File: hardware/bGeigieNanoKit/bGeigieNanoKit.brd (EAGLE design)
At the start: 104.8 x 66.7 mm, 41 parts, among them T1 2SC1815

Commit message: before removing second lcd
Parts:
- JP2: device SparkFun:1X02 -> microbuilder:1X04_ROUND
- LCD: value SSD1306_128X64_V2_LCD1.3IN_TOP -> SSD1306_128X64_V2_LCD1.3IN_LEVER; device open_hw_sockets:SSD1306_128X64_1.3IN_LCD_TOP -> open_hw_sockets:SSD1306_128X64_1.3IN_LCD_LEVER
- LCD2: value SSD1306_128X64_V2_LCD0.96IN_MIN -> SSD1306_128X64_V2_LCD0.96IN_MNT_NOOUT; device open_hw_sockets:SSD1306_128X64_0.96IN_MIN_LCD -> open_hw_sockets:SSD1306_128X64_0.96IN_LCD_MNT_NOOUT
- R8: value 47k -> 10k
- R9: value 1k -> 2.2k
- S1: device open_hw_sockets:EG1218 -> adafruit:EG1218
- moved C1 9.84 mm to (92.4, 3.17), turned to 0 degrees
- moved R9 8.82 mm to (29.8, 24.1), turned to 0 degrees
- moved JP2 6.93 mm to (18.4, 21.3)
- moved R12 4.77 mm to (61.6, 3.17)
- moved D1 3.62 mm to (42.2, 14.6)
- moved R10 3.49 mm to (45.7, 16.8)
- moved R11 3.24 mm to (86.7, 30.8)
- moved JP7 2.93 mm to (89.2, 27.3), turned to 180 degrees
- moved JP1 2.84 mm to (94.0, 11.4)
- moved SG1 1.80 mm to (28.6, 16.8)
- moved LCD 1.53 mm to (42.5, 17.7)
- moved R8 1.42 mm to (29.8, 26.7)
- moved LCD2 1.02 mm to (39.3, 16.2)
- moved C2 0.71 mm to (38.1, 40.6)
- moved U$5 0.51 mm to (79.2, 67.3)
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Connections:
- removed net N$21: FIO.JP5$12, JP4.6
- new net N$41: FIO.JP5$14, JP4.8
- net GND: now also LCD2.U$24$P$1, LCD2.U$25$P$1; no longer LCD.U$24$P$1, LCD.U$25$P$1
- net N$14: now also FIO.JP5$12, JP4.6; no longer FIO.JP5$14, JP4.8
- net N$15: no longer R4.1
- net N$33: now also R4.1
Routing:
- net N$33: track 5.72 -> 33.8 mm
- net N$15: track 27.2 -> 6.35 mm
- net VCC: track 219.5 -> 210.8 mm
- net N$14: track 24.6 -> 30.5 mm
- net N$41: track 0.00 -> 5.72 mm
- net N$21: track 5.72 -> 0.00 mm
- net N$26: track 3.49 -> 8.94 mm
- net N$20: track 47.8 -> 52.7 mm
- net N$23: track 11.8 -> 16.6 mm
- net N$29: track 11.3 -> 6.71 mm
- net N$31: track 6.88 -> 3.31 mm
- net N$24: track 9.42 -> 12.8 mm
- net N$25: track 16.9 -> 14.4 mm
- net N$32: track 51.9 -> 53.7 mm
- net N$4: track 37.4 -> 35.8 mm
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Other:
- board text added: "Audio"
- board text added: "bGeigie Nano Kit v1.0r2"
- board text removed: "Audio Out"
- board text removed: "bGeigie Nano Kit v1.0"

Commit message: applied most all changes rc v1.0r2
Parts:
- removed CHARGE: RED, adafruit:LED3MM
- removed JP7: (no value), microbuilder:JUMPER2
- removed LCD2: SSD1306_128X64_V2_LCD0.96IN_MNT_NOOUT, open_hw_sockets:SSD1306_128X64_0.96IN_LCD_MNT_NOOUT
- removed R11: 1k, rcl:0207/10
- added U$1: (no value), open_hw_sockets:SAFECAST_LOGO4
- C1, C2, C3: device rcl:C050-024X044 -> rcl:C025-024X044
- moved JP2 5.08 mm to (18.4, 16.2)
- moved C3 3.49 mm to (47.3, 25.7)
- moved C2 3.18 mm to (36.2, 43.2), turned to 90 degrees
- moved SG1 2.88 mm to (31.4, 16.5)
- moved D1 1.93 mm to (41.9, 16.5)
- moved C1 1.59 mm to (93.3, 4.45)
- moved S5 1.14 mm to (7.30, 14.0)
- moved JP1 1.14 mm to (94.6, 12.4)
- moved LCD 0.70 mm to (43.2, 17.7)
- moved JP4 0.32 mm to (59.7, 49.8)
- turned R4 to 90 degrees
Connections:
- removed net N$29: JP7.1, R11.1
- removed net N$31: CHARGE.K, R11.2
- net GND: no longer JP7.2, LCD2.JP1$8, LCD2.U$24$P$1, LCD2.U$25$P$1
- net N$1: no longer LCD2.JP1$1
- net N$2: no longer LCD2.JP1$2
- net N$3: no longer LCD2.JP1$3
- net N$4: no longer LCD2.JP1$5
- net N$5: no longer LCD2.JP1$4
- net VCC: no longer LCD2.JP1$7
- net VIN: no longer CHARGE.A
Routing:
- net N$17: track 31.5 -> 21.8 mm
- net N$29: track 6.71 -> 0.00 mm
- net VIN: track 17.4 -> 12.6 mm
- net N$27: track 30.4 -> 26.3 mm
- net N$31: track 3.31 -> 0.00 mm
- net N$24: track 12.8 -> 15.4 mm
- net N$23: track 16.6 -> 14.3 mm
- net N$18: track 76.4 -> 74.2 mm
- net N$25: track 14.4 -> 16.5 mm
- net N$33: track 33.8 -> 35.2 mm
- net N$32: track 53.7 -> 52.5 mm
- net N$20: track 52.7 -> 51.6 mm
- net N$4: track 35.8 -> 35.1 mm
- net N$2: track 42.3 -> 41.6 mm
- net N$5: track 32.5 -> 31.8 mm
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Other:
- board text added: "Audio out"
- board text added: "Special thanks to: Joe,Rob,Jurgen,Sean,Robin,Akiba,Azby Shigeru,Joi,Dan,Peter,Joseph,Medcom,Loftwork,FabCafe Pelican,Tokyo Hacker Space,CRASH Space,Adafruit,Sparkfun"
- board text added: "bGeigie Nano Kit"
- board text added: "bGeigie Nano v1.0r2"
- board text removed: "Audio"
- board text removed: "Special thanks to: Joe, Rob, Jurgen, Sean, Robin, Akiba, Shigeru, Joi, Dan, Medcom, Loftwork, FabCafe, Pelican, Tokyo Hacker Space, CRASH Space, Adafruit, Sparkfun"
- board text removed: "bGeigie Nano Kit v1.0r2"

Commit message: finishing change set for rev2
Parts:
- S1: value (none) -> EG1206; device adafruit:EG1218 -> open_hw_sockets:EG1206
- moved S1 2.13 mm to (90.8, 62.5)
- moved OPENLOG 0.64 mm to (86.7, 25.1)
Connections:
- removed net VIN: FIO.JP6$2
- net GND: now also S1.MT1, S1.MT2
- net N$12: now also S1.2; no longer S1.P
- net N$13: now also S1.3; no longer S1.S
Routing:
- net VIN: track 12.6 -> 0.00 mm
- net VCC: track 211.0 -> 210.4 mm
- net N$9: track 31.2 -> 30.6 mm
- net N$8: track 34.8 -> 34.2 mm
- net N$10: track 27.6 -> 27.0 mm
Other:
- board text added: "bGeigie Nano Kit v1.0r2"
- board text removed: "bGeigie Nano v1.0r2"
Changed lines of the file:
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@@
 <layer number="29" name="tStop" color="7" fill="3" visible="yes" active="yes"/>
 <layer number="30" name="bStop" color="7" fill="6" visible="yes" active="yes"/>
-<layer number="31" name="tCream" color="7" fill="4" visible="yes" active="yes"/>
-<layer number="32" name="bCream" color="7" fill="5" visible="yes" active="yes"/>
+<layer number="31" name="tCream" color="7" fill="4" visible="no" active="yes"/>
+<layer number="32" name="bCream" color="7" fill="5" visible="no" active="yes"/>
 <layer number="33" name="tFinish" color="6" fill="3" visible="yes" active="yes"/>
 <layer number="34" name="bFinish" color="6" fill="6" visible="yes" active="yes"/>
-<layer number="35" name="tGlue" color="7" fill="4" visible="yes" active="yes"/>
-<layer number="36" name="bGlue" color="7" fill="5" visible="yes" active="yes"/>
+<layer number="35" name="tGlue" color="7" fill="4" visible="no" active="yes"/>
+<layer number="36" name="bGlue" color="7" fill="5" visible="no" active="yes"/>
 <layer number="37" name="tTest" color="7" fill="1" visible="yes" active="yes"/>
 <layer number="38" name="bTest" color="7" fill="1" visible="yes" active="yes"/>
@@
 <vertex x="38.1" y="40.64"/>
 </polygon>
-<text x="8.5725" y="57.4675" size="2.54" layer="22" font="vector" ratio="10" distance="40" rot="SMR270">bGeigie Nano v1.0r2</text>
+<text x="7.9375" y="58.1025" size="2.54" layer="22" font="vector" ratio="10" distance="40" rot="SMR270">bGeigie Nano Kit v1.0r2</text>
 </plain>
 <attributes>
@@
 </element>
 <element name="S5" library="SparkFun" package="TACTILE-PTH" value="" x="7.3025" y="13.97" smashed="yes" rot="R180"/>
-<element name="S1" library="adafruit" package="EG1218" value="" x="88.9" y="63.5" smashed="yes" rot="SR180">
-<attribute name="NAME" x="89.789" y="60.6425" size="1.27" layer="25" font="vector" rot="SR180"/>
-</element>
 <element name="SG1" library="SparkFun" package="BUZZER-12MM" value="BUZZER" x="31.4325" y="16.51" smashed="yes" rot="R180">
 <attribute name="NAME" x="33.972503125" y="13.97" size="0.6096" layer="25" ratio="10" rot="R180" display="off"/>
@@
 <attribute name="VALUE" x="34.29" y="53.848" size="1.27" layer="27" ratio="10" display="off"/>
 </element>
-<element name="OPENLOG" library="open_hw_sockets" package="OPENLOG" value="OPENLOG" x="87.3125" y="25.0825" smashed="yes" rot="R270">
-<attribute name="NAME" x="96.9645" y="23.8125" size="2.54" layer="25" rot="SR270" display="off"/>
+<element name="OPENLOG" library="open_hw_sockets" package="OPENLOG" value="OPENLOG" x="86.6775" y="25.0825" smashed="yes" rot="R270">
+<attribute name="NAME" x="96.3295" y="23.8125" size="2.54" layer="25" rot="SR270" display="off"/>
 </element>
 <element name="SW1" library="special" package="EDG-02" value="" x="17.145" y="64.135" smashed="yes" rot="SR90">
@@
 </element>
 <element name="U$1" library="open_hw_sockets" package="SAFECAST_LOGO4" value="" x="50.8" y="50.8" rot="MR270"/>
+<element name="S1" library="open_hw_sockets" package="EG1206" value="EG1206" x="90.805" y="62.5475" rot="R180"/>
 </elements>
 <signals>
@@
 </polygon>
 <contactref element="JP2" pad="2"/>
+<contactref element="S1" pad="MT1"/>
+<contactref element="S1" pad="MT2"/>
 </signal>
 <signal name="VCC" class="1">
@@
 <wire x1="68.58" y1="60.96" x2="69.85" y2="59.69" width="1.4224" layer="1"/>
 <wire x1="69.85" y1="59.69" x2="69.85" y2="55.88" width="1.4224" layer="1"/>
-<wire x1="85.4075" y1="16.1925" x2="88.5825" y2="16.1925" width="1.4224" layer="16"/>
+<wire x1="85.4075" y1="16.1925" x2="87.9475" y2="16.1925" width="1.4224" layer="16"/>
 <wire x1="29.845" y1="38.4175" x2="29.845" y2="41.275" width="1.4224" layer="16"/>
 <wire x1="29.845" y1="41.275" x2="26.67" y2="44.45" width="1.4224" layer="16"/>
@@
 <wire x1="52.832" y1="9.525" x2="57.785" y2="9.525" width="1.4224" layer="1"/>
 <wire x1="77.47" y1="7.62" x2="86.0425" y2="16.1925" width="1.4224" layer="1"/>
-<wire x1="86.0425" y1="16.1925" x2="88.5825" y2="16.1925" width="1.4224" layer="1"/>
+<wire x1="86.0425" y1="16.1925" x2="87.9475" y2="16.1925" width="1.4224" layer="1"/>
 <wire x1="85.4075" y1="16.1925" x2="78.74" y2="22.86" width="1.4224" layer="16"/>
 <wire x1="78.74" y1="22.86" x2="78.74" y2="29.21" width="1.4224" layer="16"/>
@@
 <wire x1="97.155" y1="8.5725" x2="97.155" y2="12.065" width="1.4224" layer="1"/>
 <wire x1="97.155" y1="12.065" x2="93.0275" y2="16.1925" width="1.4224" layer="1"/>
-<wire x1="93.0275" y1="16.1925" x2="88.5825" y2="16.1925" width="1.4224" layer="1"/>
+<wire x1="93.0275" y1="16.1925" x2="87.9475" y2="16.1925" width="1.4224" layer="1"/>
 <wire x1="97.155" y1="8.5725" x2="97.155" y2="6.985" width="1.4224" layer="1"/>
 <wire x1="97.155" y1="6.985" x2="94.615" y2="4.445" width="1.4224" layer="1"/>
@@
 <contactref element="OPENLOG" pad="JP1$3"/>
 <wire x1="59.69" y1="33.02" x2="73.9775" y2="18.7325" width="0.6096" layer="1"/>
-<wire x1="73.9775" y1="18.7325" x2="88.5825" y2="18.7325" width="0.6096" layer="1"/>
+<wire x1="73.9775" y1="18.7325" x2="87.9475" y2="18.7325" width="0.6096" layer="1"/>
 </signal>
 <signal name="N$9">
@@
 <contactref element="OPENLOG" pad="JP1$2"/>
 <wire x1="62.23" y1="33.02" x2="73.9775" y2="21.2725" width="0.6096" layer="1"/>
-<wire x1="73.9775" y1="21.2725" x2="88.5825" y2="21.2725" width="0.6096" layer="1"/>
+<wire x1="73.9775" y1="21.2725" x2="87.9475" y2="21.2725" width="0.6096" layer="1"/>
 </signal>
 <signal name="N$10">
@@
 <contactref element="OPENLOG" pad="JP1$1"/>
 <wire x1="64.77" y1="33.02" x2="73.9775" y2="23.8125" width="0.6096" layer="1"/>
-<wire x1="73.9775" y1="23.8125" x2="88.5825" y2="23.8125" width="0.6096" layer="1"/>
+<wire x1="73.9775" y1="23.8125" x2="87.9475" y2="23.8125" width="0.6096" layer="1"/>
 </signal>
 <signal name="N$12" class="2">
 <contactref element="FIO" pad="JP7$2"/>
-<contactref element="S1" pad="P"/>
-<wire x1="82.55" y1="47.625" x2="82.55" y2="53.34" width="1.4224" layer="1"/>
-<wire x1="82.55" y1="53.34" x2="88.9" y2="59.69" width="1.4224" layer="1"/>
-<wire x1="88.9" y1="59.69" x2="88.9" y2="63.5" width="1.4224" layer="1"/>
-</signal>
-<signal name="VIN">
-<contactref element="FIO" pad="JP6$2"/>
-<wire x1="93.98" y1="41.91" x2="92.71" y2="41.91" width="0.6096" layer="1"/>
-<wire x1="92.71" y1="41.91" x2="91.44" y2="40.64" width="0.6096" layer="1"/>
-<wire x1="91.44" y1="40.64" x2="91.44" y2="35.56" width="0.6096" layer="1"/>
-<wire x1="91.44" y1="35.56" x2="94.615" y2="32.385" width="0.6096" layer="1"/>
+<wire x1="90.805" y1="55.88" x2="82.55" y2="47.625" width="1.4224" layer="1"/>
+<contactref element="S1" pad="2"/>
+<wire x1="90.805" y1="55.88" x2="90.805" y2="62.5475" width="1.4224" layer="1"/>
 </signal>
 <signal name="VBATT">
 <contactref element="FIO" pad="JP2$2"/>
 <contactref element="R1" pad="1"/>
-<wire x1="93.98" y1="50.8" x2="85.725" y2="59.055" width="0.6096" layer="16"/>
-<wire x1="85.725" y1="59.055" x2="66.04" y2="59.055" width="0.6096" layer="16"/>
 <contactref element="JP6" pad="1"/>
 <via x="76.2" y="26.67" extent="1-16" drill="0.6"/>
@@
 <wire x1="85.09" y1="43.18" x2="92.71" y2="50.8" width="0.6096" layer="1"/>
 <wire x1="92.71" y1="50.8" x2="93.98" y2="50.8" width="0.6096" layer="1"/>
+<wire x1="66.04" y1="59.055" x2="76.835" y2="59.055" width="0.6096" layer="16"/>
+<wire x1="76.835" y1="59.055" x2="85.09" y2="50.8" width="0.6096" layer="16"/>
+<wire x1="85.09" y1="50.8" x2="93.98" y2="50.8" width="0.6096" layer="16"/>
 </signal>
 <signal name="N$13" class="2">
 <contactref element="FIO" pad="JP7$1"/>
-<contactref element="S1" pad="S"/>
-<wire x1="86.36" y1="63.5" x2="86.36" y2="62.23" width="1.4224" layer="1"/>
-<wire x1="86.36" y1="62.23" x2="80.01" y2="55.88" width="1.4224" layer="1"/>
-<wire x1="80.01" y1="47.625" x2="80.01" y2="55.88" width="1.4224" layer="1"/>
+<wire x1="87.805" y1="57.325" x2="80.01" y2="49.53" width="1.4224" layer="1"/>
+<wire x1="80.01" y1="49.53" x2="80.01" y2="47.625" width="1.4224" layer="1"/>
+<contactref element="S1" pad="3"/>
+<wire x1="87.805" y1="57.325" x2="87.805" y2="62.5475" width="1.4224" layer="1"/>
 </signal>
 <signal name="N$11">
@@
 </signal>
 </signals>
+<errors>
+</errors>
 </board>
 </drawing>

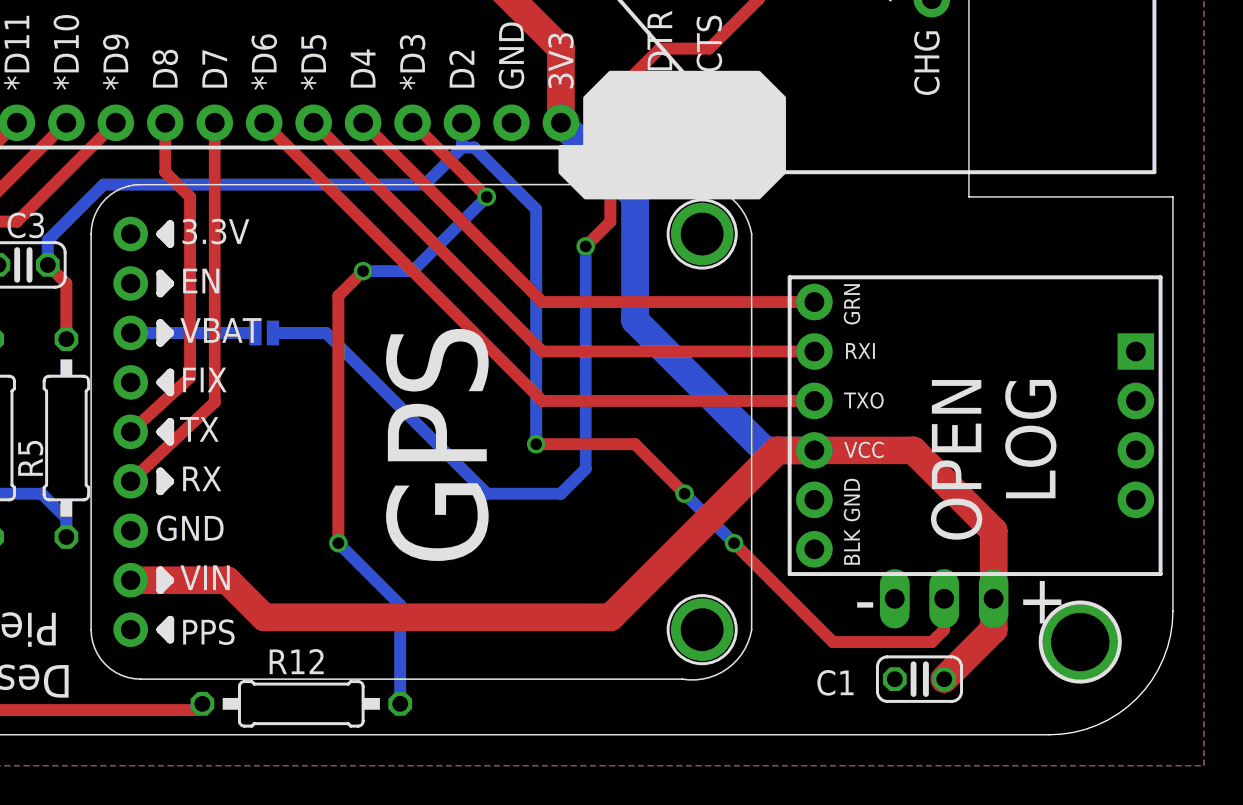
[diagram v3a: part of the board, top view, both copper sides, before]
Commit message: adding more space between irover plug and post
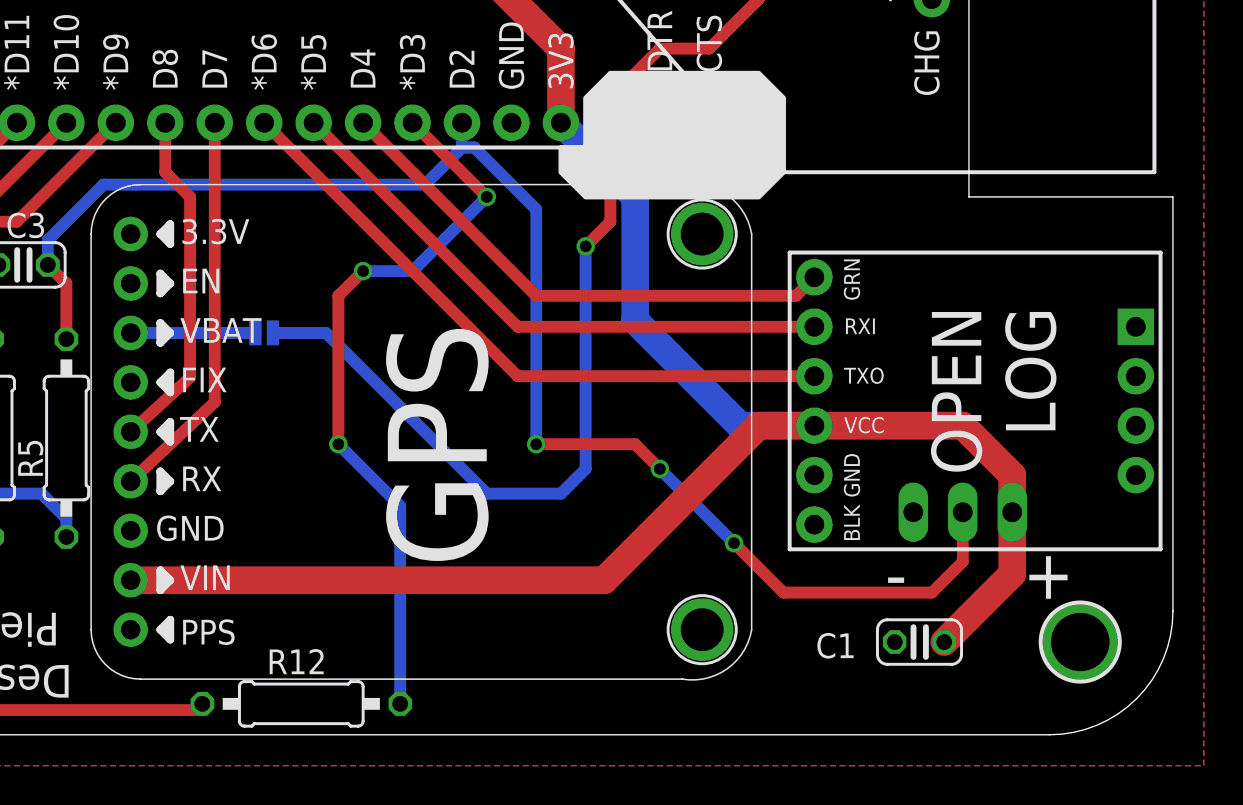
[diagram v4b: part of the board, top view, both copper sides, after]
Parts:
- moved JP1 4.55 mm to (95.6, 16.8)
- moved C1 1.90 mm to (93.3, 6.35)
- moved OPENLOG 1.27 mm to (86.7, 26.4)
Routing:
- net N$18: track 74.2 -> 75.4 mm
- net N$9: track 30.6 -> 30.1 mm
- net N$8: track 34.2 -> 33.6 mm
